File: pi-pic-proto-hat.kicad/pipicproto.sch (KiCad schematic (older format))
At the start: 34 parts, among them J1 RUN/~PGM~, J10 Conn_01x13_Male, J11 Conn_5P_2, J12 Conn_01x01_Male, J2 Conn_SW1, J22 Conn_01x13_Male, J3 Conn_5P, J4 Conn_3V3P, J5 Conn_3V3P_2, J6 Barrel_Jack_Switch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

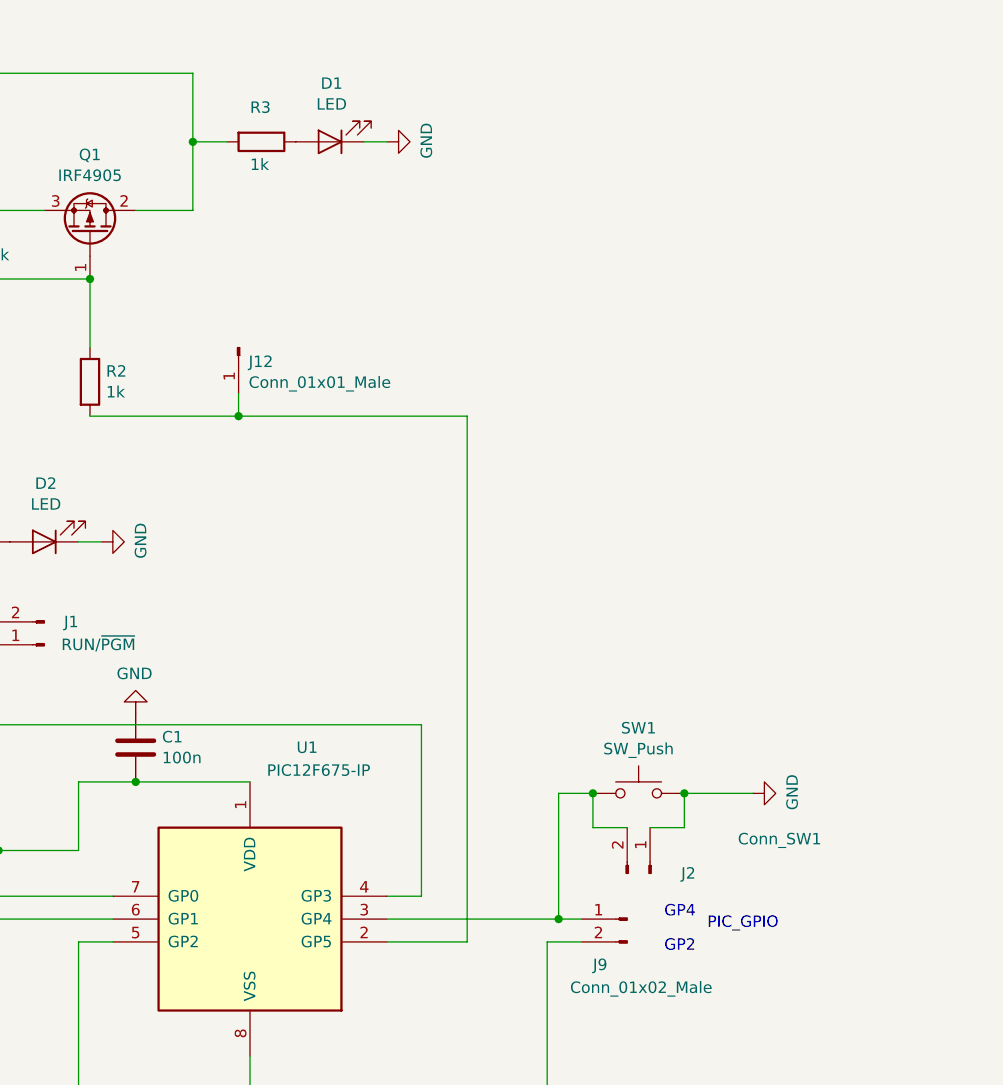
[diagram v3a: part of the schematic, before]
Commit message: V2.20: added DS3231
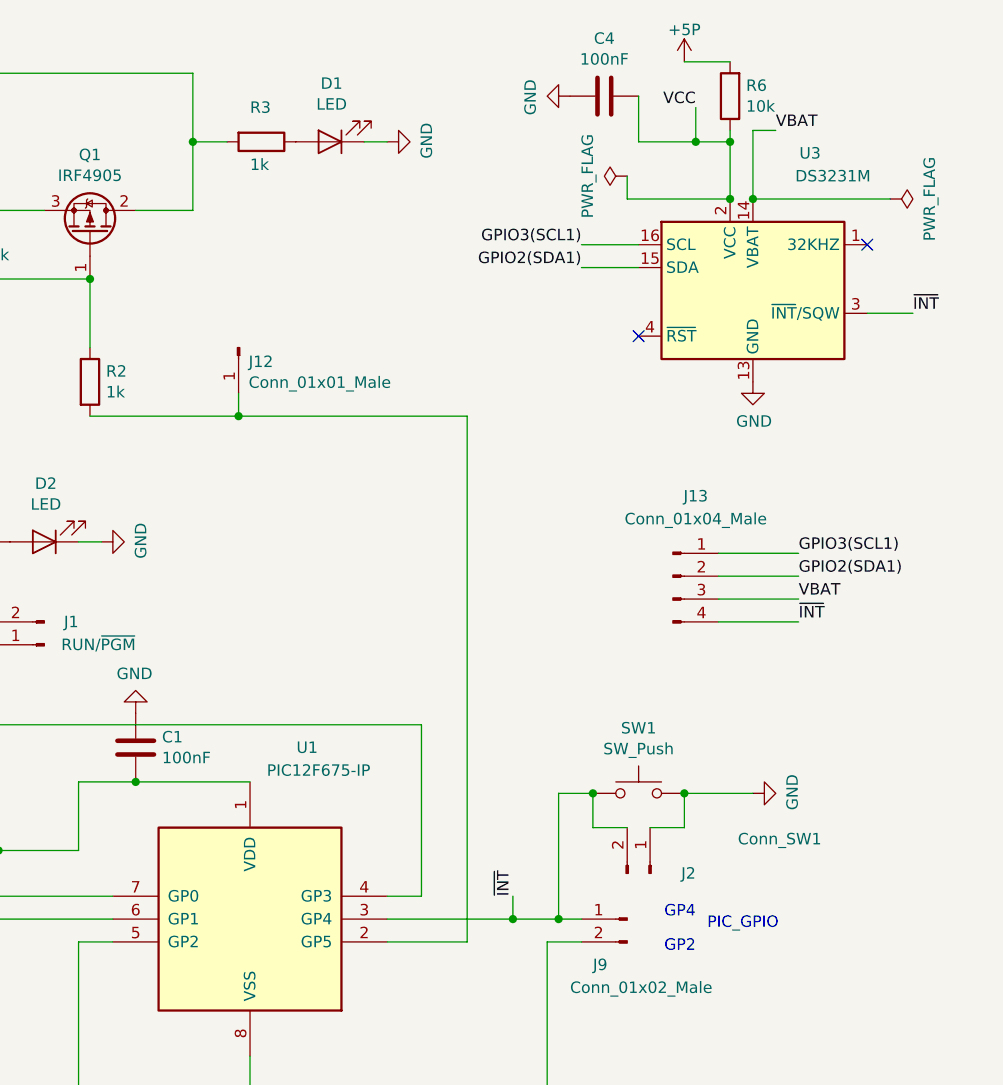
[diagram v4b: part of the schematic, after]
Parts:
- added C4: 100nF, Capacitor_SMD:C_1206_3216Metric_Pad1.42x1.75mm_HandSolder, symbol Device:C
- added J13: Conn_01x04_Male, Connector_PinHeader_2.54mm:PinHeader_1x04_P2.54mm_Vertical, symbol Connector:Conn_01x04_Male
- added R6: 10k, Resistor_SMD:R_1206_3216Metric_Pad1.42x1.75mm_HandSolder, symbol Device:R
- added U3: DS3231M, Package_SO:SOIC-16W_7.5x10.3mm_P1.27mm, symbol Timer_RTC:DS3231M
- C1: value 100n -> 100nF
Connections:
- net +5P: now also R6.2
- net GND: now also C4.2, U3.10 (GND), U3.11 (GND), U3.12 (GND), U3.13 (GND), U3.5 (GND), U3.6 (GND), U3.7 (GND), U3.8 (GND), U3.9 (GND)
- net GPIO2(SDA1): now also J13.2 (Pin_2), U3.15 (SDA)
- net GPIO3(SCL1): now also J13.1 (Pin_1), U3.16 (SCL)
- net ~INT: now reaches J2.2 (Pin_2), J9.1 (Pin_1), SW1.1, U1.3 (GP4)
- net ~INT: now also J13.4 (Pin_4), U3.3 (~INT~/SQW)
- new net VBAT: J13.3 (Pin_3), U3.14 (VBAT)
- new net VCC: C4.1, R6.1, U3.2 (VCC)
- no-connect marks 4 -> 6
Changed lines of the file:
@@
 Sheet 1 1
 Title "PI PIC Prototyping Area"
-Date "2020-07-25"
-Rev "2.19"
+Date "2020-07-30"
+Rev "2.20"
 Comp "Bernhard Bablok, Lothar Hiller"
 Comment1 "https://github.com/bablokb/pi-pic-proto-hat"
@@
 P 7500 3850
 F 0 "C1" H 7615 3896 50  0000 L CNN
-F 1 "100n" H 7615 3805 50  0000 L CNN
+F 1 "100nF" H 7615 3805 50  0000 L CNN
 F 2 "Capacitor_SMD:C_1206_3216Metric_Pad1.42x1.75mm_HandSolder" H 7538 3700 50  0001 C CNN
 F 3 "~" H 7500 3850 50  0001 C CNN
@@
 $EndComp
 Wire Wire Line
-	8600 4600 9350 4600
+	8600 4600 9150 4600
 Wire Wire Line
 	9300 5750 9300 4700
@@
 Wire Wire Line
 	7950 2400 7300 2400
+$Comp
+L Timer_RTC:DS3231M U3
+U 1 1 5F238501
+P 10200 1850
+F 0 "U3" H 10450 2450 50  0000 C CNN
+F 1 "DS3231M" H 10550 2350 50  0000 C CNN
+F 2 "Package_SO:SOIC-16W_7.5x10.3mm_P1.27mm" H 10200 1250 50  0001 C CNN
+F 3 "http://datasheets.maximintegrated.com/en/ds/DS3231.pdf" H 10470 1900 50  0001 C CNN
+	1    10200 1850
+	1    0    0    -1
+$EndComp
+$Comp
+L Connector:Conn_01x04_Male J13
+U 1 1 5F2395D8
+P 9850 3100
+F 0 "J13" H 9950 3450 50  0000 C CNN
+F 1 "Conn_01x04_Male" H 9950 3350 50  0000 C CNN
+F 2 "Connector_PinHeader_2.54mm:PinHeader_1x04_P2.54mm_Vertical" H 9850 3100 50  0001 C CNN
+F 3 "~" H 9850 3100 50  0001 C CNN
+	1    9850 3100
+	1    0    0    -1
+$EndComp
+Text Label 10400 3100 0    50   ~ 0
+GPIO2(SDA1)
+Text Label 10400 3000 0    50   ~ 0
+GPIO3(SCL1)
+Text Label 9450 1750 2    50   ~ 0
+GPIO2(SDA1)
+Text Label 9450 1650 2    50   ~ 0
+GPIO3(SCL1)
+Text Label 10400 3300 0    50   ~ 0
+~INT
+Text Label 10900 1950 0    50   ~ 0
+~INT
+NoConn ~ 10700 1650
+$Comp
+L power:GND #PWR013
+U 1 1 5F24DB44
+P 10200 2250
+F 0 "#PWR013" H 10200 2000 50  0001 C CNN
+F 1 "GND" H 10205 2077 50  0000 C CNN
+F 2 "" H 10200 2250 50  0001 C CNN
+F 3 "" H 10200 2250 50  0001 C CNN
+	1    10200 2250
+	1    0    0    -1
+$EndComp
+NoConn ~ 9700 2050
+$Comp
+L Device:R R6
+U 1 1 5F25761B
+P 10100 1000
+F 0 "R6" H 10030 954 50  0000 R CNN
+F 1 "10k" H 10030 1045 50  0000 R CNN
+F 2 "Resistor_SMD:R_1206_3216Metric_Pad1.42x1.75mm_HandSolder" V 10030 1000 50  0001 C CNN
+F 3 "~" H 10100 1000 50  0001 C CNN
+	1    10100 1000
+	-1   0    0    1
+$EndComp
+$Comp
+L power:+5P #PWR012
+U 1 1 5F26109E
+P 9900 850
+F 0 "#PWR012" H 9900 700 50  0001 C CNN
+F 1 "+5P" H 9900 990 50  0000 C CNN
+F 2 "" H 9900 850 50  0000 C CNN
+F 3 "" H 9900 850 50  0000 C CNN
+	1    9900 850
+	1    0    0    -1
+$EndComp
+Wire Wire Line
+	9900 850  10100 850
+Wire Wire Line
+	10700 1950 10900 1950
+Wire Wire Line
+	10050 3100 10400 3100
+Wire Wire Line
+	10050 3000 10400 3000
+Wire Wire Line
+	9700 1650 9450 1650
+Wire Wire Line
+	9700 1750 9450 1750
+Text Label 10400 3200 0    50   ~ 0
+VBAT
+Text Label 10300 1150 0    50   ~ 0
+VBAT
+Wire Wire Line
+	10200 1450 10200 1150
+Wire Wire Line
+	10200 1150 10300 1150
+Wire Wire Line
+	10400 3200 10050 3200
+Text Label 9950 1050 2    50   ~ 0
+VCC
+Wire Wire Line
+	10050 3300 10400 3300
+$Comp
+L power:PWR_FLAG #FLG0103
+U 1 1 5F2E32E1
+P 9650 1350
+F 0 "#FLG0103" H 9650 1425 50  0001 C CNN
+F 1 "PWR_FLAG" H 9650 1523 50  0000 C CNN
+F 2 "" H 9650 1350 50  0001 C CNN
+F 3 "~" H 9650 1350 50  0001 C CNN
+	1    9650 1350
+	0    -1   -1   0
+$EndComp
+Wire Wire Line
+	9650 1350 9650 1450
+Wire Wire Line
+	9650 1450 10100 1450
+Connection ~ 10100 1450
+$Comp
+L power:PWR_FLAG #FLG0104
+U 1 1 5F2EE834
+P 10800 1450
+F 0 "#FLG0104" H 10800 1525 50  0001 C CNN
+F 1 "PWR_FLAG" H 10800 1623 50  0000 C CNN
+F 2 "" H 10800 1450 50  0001 C CNN
+F 3 "~" H 10800 1450 50  0001 C CNN
+	1    10800 1450
+	0    1    1    0
+$EndComp
+Wire Wire Line
+	10800 1450 10200 1450
+Connection ~ 10200 1450
+$Comp
+L Device:C C4
+U 1 1 5F313C7C
+P 9550 1000
+F 0 "C4" V 9298 1000 50  0000 C CNN
+F 1 "100nF" V 9389 1000 50  0000 C CNN
+F 2 "Capacitor_SMD:C_1206_3216Metric_Pad1.42x1.75mm_HandSolder" H 9588 850 50  0001 C CNN
+F 3 "~" H 9550 1000 50  0001 C CNN
+	1    9550 1000
+	0    1    1    0
+$EndComp
+Wire Wire Line
+	10100 1150 10100 1200
+Wire Wire Line
+	9950 1050 9950 1200
+Wire Wire Line
+	9950 1200 10100 1200
+Connection ~ 10100 1200
+Wire Wire Line
+	10100 1200 10100 1450
+Wire Wire Line
+	9700 1000 9700 1200
+Wire Wire Line
+	9700 1200 9950 1200
+Connection ~ 9950 1200
+$Comp
+L power:GND #PWR023
+U 1 1 5F34D64A
+P 9400 1000
+F 0 "#PWR023" H 9400 750 50  0001 C CNN
+F 1 "GND" H 9405 827 50  0000 C CNN
+F 2 "" H 9400 1000 50  0001 C CNN
+F 3 "" H 9400 1000 50  0001 C CNN
+	1    9400 1000
+	0    1    1    0
+$EndComp
+Text Label 9150 4500 1    50   ~ 0
+~INT
+Wire Wire Line
+	9150 4500 9150 4600
+Connection ~ 9150 4600
+Wire Wire Line
+	9150 4600 9350 4600
 $EndSCHEMATC

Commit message: V2.21: added 32KHZ-pin of RTC to connector
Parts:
- J13: value Conn_01x04_Male -> Conn_01x05_Male; footprint Connector_PinHeader_2.54mm:PinHeader_1x04_P2.54mm_Vertical -> Connector_PinHeader_2.54mm:PinHeader_1x05_P2.54mm_Vertical; symbol Connector:Conn_01x04_Male -> Connector:Conn_01x05_Male
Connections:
- net 32KHZ: now reaches U3.1 (32KHZ)
- net 32KHZ: now also J13.5 (Pin_5)
- no-connect marks 6 -> 5
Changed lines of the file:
@@
 Sheet 1 1
 Title "PI PIC Prototyping Area"
-Date "2020-07-30"
-Rev "2.20"
+Date "2020-08-01"
+Rev "2.21"
 Comp "Bernhard Bablok, Lothar Hiller"
 Comment1 "https://github.com/bablokb/pi-pic-proto-hat"
@@
 U 1 1 5F238501
 P 10200 1850
-F 0 "U3" H 10450 2450 50  0000 C CNN
-F 1 "DS3231M" H 10550 2350 50  0000 C CNN
+F 0 "U3" H 10350 2300 50  0000 C CNN
+F 1 "DS3231M" H 10450 2200 50  0000 C CNN
 F 2 "Package_SO:SOIC-16W_7.5x10.3mm_P1.27mm" H 10200 1250 50  0001 C CNN
 F 3 "http://datasheets.maximintegrated.com/en/ds/DS3231.pdf" H 10470 1900 50  0001 C CNN
@@
 $EndComp
 $Comp
-L Connector:Conn_01x04_Male J13
+L Connector:Conn_01x05_Male J13
 U 1 1 5F2395D8
-P 9850 3100
-F 0 "J13" H 9950 3450 50  0000 C CNN
-F 1 "Conn_01x04_Male" H 9950 3350 50  0000 C CNN
-F 2 "Connector_PinHeader_2.54mm:PinHeader_1x04_P2.54mm_Vertical" H 9850 3100 50  0001 C CNN
-F 3 "~" H 9850 3100 50  0001 C CNN
-	1    9850 3100
+P 9850 3200
+F 0 "J13" H 9950 3600 50  0000 C CNN
+F 1 "Conn_01x05_Male" H 9950 3500 50  0000 C CNN
+F 2 "Connector_PinHeader_2.54mm:PinHeader_1x05_P2.54mm_Vertical" H 9850 3200 50  0001 C CNN
+F 3 "~" H 9850 3200 50  0001 C CNN
+	1    9850 3200
 	1    0    0    -1
 $EndComp
@@
 Text Label 10900 1950 0    50   ~ 0
 ~INT
-NoConn ~ 10700 1650
 $Comp
 L power:GND #PWR013
@@
 P 10800 1450
 F 0 "#FLG0104" H 10800 1525 50  0001 C CNN
-F 1 "PWR_FLAG" H 10800 1623 50  0000 C CNN
+F 1 "PWR_FLAG" V 10700 1600 50  0000 C CNN
 F 2 "" H 10800 1450 50  0001 C CNN
 F 3 "~" H 10800 1450 50  0001 C CNN
@@
 Wire Wire Line
 	9150 4600 9350 4600
+Text Label 10400 3400 0    50   ~ 0
+32KHZ
+Wire Wire Line
+	10050 3400 10400 3400
+Text Label 10900 1650 0    50   ~ 0
+32KHZ
+Wire Wire Line
+	10700 1650 10900 1650
 $EndSCHEMATC

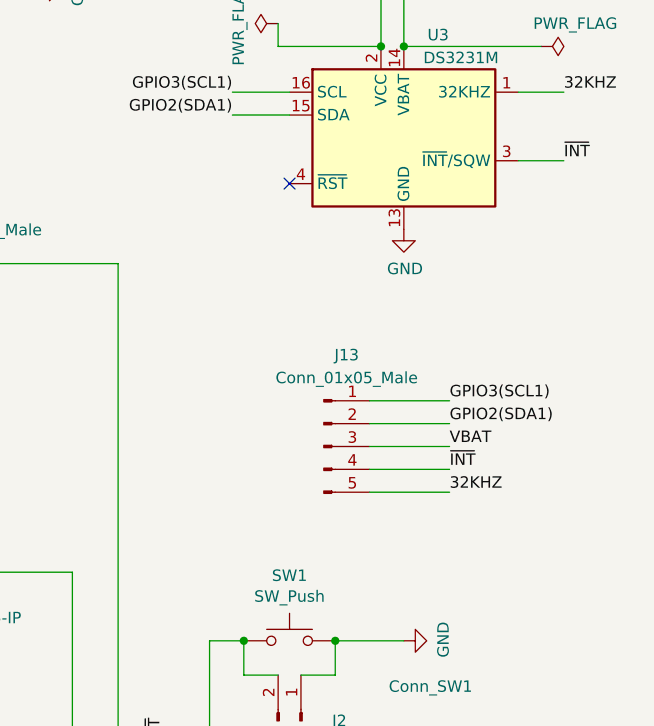
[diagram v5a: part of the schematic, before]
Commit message: V2.22: added RST/GND connector for RTC
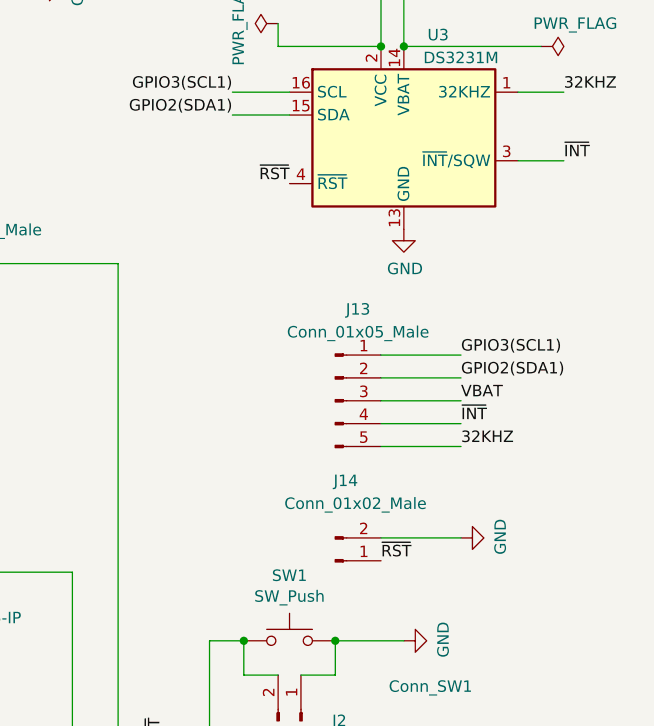
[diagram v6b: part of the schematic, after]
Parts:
- added J14: Conn_01x02_Male, Connector_PinHeader_2.54mm:PinHeader_1x02_P2.54mm_Vertical, symbol Connector:Conn_01x02_Male
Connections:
- net GND: now also J14.2 (Pin_2)
- net ~RST: now reaches U3.4 (~RST)
- net ~RST: now also J14.1 (Pin_1)
- no-connect marks 5 -> 4
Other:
- moved on the sheet: J13
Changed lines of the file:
@@
 Title "PI PIC Prototyping Area"
 Date "2020-08-01"
-Rev "2.21"
+Rev "2.22"
 Comp "Bernhard Bablok, Lothar Hiller"
 Comment1 "https://github.com/bablokb/pi-pic-proto-hat"
@@
 L Connector:Conn_01x05_Male J13
 U 1 1 5F2395D8
-P 9850 3200
-F 0 "J13" H 9950 3600 50  0000 C CNN
-F 1 "Conn_01x05_Male" H 9950 3500 50  0000 C CNN
-F 2 "Connector_PinHeader_2.54mm:PinHeader_1x05_P2.54mm_Vertical" H 9850 3200 50  0001 C CNN
-F 3 "~" H 9850 3200 50  0001 C CNN
-	1    9850 3200
-	1    0    0    -1
-$EndComp
-Text Label 10400 3100 0    50   ~ 0
+P 9900 3000
+F 0 "J13" H 10000 3400 50  0000 C CNN
+F 1 "Conn_01x05_Male" H 10000 3300 50  0000 C CNN
+F 2 "Connector_PinHeader_2.54mm:PinHeader_1x05_P2.54mm_Vertical" H 9900 3000 50  0001 C CNN
+F 3 "~" H 9900 3000 50  0001 C CNN
+	1    9900 3000
+	1    0    0    -1
+$EndComp
+Text Label 10450 2900 0    50   ~ 0
 GPIO2(SDA1)
-Text Label 10400 3000 0    50   ~ 0
+Text Label 10450 2800 0    50   ~ 0
 GPIO3(SCL1)
 Text Label 9450 1750 2    50   ~ 0
@@
 Text Label 9450 1650 2    50   ~ 0
 GPIO3(SCL1)
-Text Label 10400 3300 0    50   ~ 0
+Text Label 10450 3100 0    50   ~ 0
 ~INT
 Text Label 10900 1950 0    50   ~ 0
@@
 	1    0    0    -1
 $EndComp
-NoConn ~ 9700 2050
 $Comp
 L Device:R R6
@@
 	10700 1950 10900 1950
 Wire Wire Line
-	10050 3100 10400 3100
-Wire Wire Line
-	10050 3000 10400 3000
+	10100 2900 10450 2900
+Wire Wire Line
+	10100 2800 10450 2800
 Wire Wire Line
 	9700 1650 9450 1650
 Wire Wire Line
 	9700 1750 9450 1750
-Text Label 10400 3200 0    50   ~ 0
+Text Label 10450 3000 0    50   ~ 0
 VBAT
 Text Label 10300 1150 0    50   ~ 0
@@
 	10200 1150 10300 1150
 Wire Wire Line
-	10400 3200 10050 3200
+	10450 3000 10100 3000
 Text Label 9950 1050 2    50   ~ 0
 VCC
 Wire Wire Line
-	10050 3300 10400 3300
+	10100 3100 10450 3100
 $Comp
 L power:PWR_FLAG #FLG0103
@@
 Wire Wire Line
 	9150 4600 9350 4600
-Text Label 10400 3400 0    50   ~ 0
+Text Label 10450 3200 0    50   ~ 0
 32KHZ
 Wire Wire Line
-	10050 3400 10400 3400
+	10100 3200 10450 3200
 Text Label 10900 1650 0    50   ~ 0
 32KHZ
 Wire Wire Line
 	10700 1650 10900 1650
+$Comp
+L Connector:Conn_01x02_Male J14
+U 1 1 5F2F400C
+P 9900 3700
+F 0 "J14" H 10000 3350 50  0000 R CNN
+F 1 "Conn_01x02_Male" H 10300 3450 50  0000 R CNN
+F 2 "Connector_PinHeader_2.54mm:PinHeader_1x02_P2.54mm_Vertical" H 9900 3700 50  0001 C CNN
+F 3 "~" H 9900 3700 50  0001 C CNN
+	1    9900 3700
+	1    0    0    1
+$EndComp
+Text Label 10100 3700 0    50   ~ 0
+~RST
+$Comp
+L power:GND #PWR022
+U 1 1 5F3365CF
+P 10450 3600
+F 0 "#PWR022" H 10450 3350 50  0001 C CNN
+F 1 "GND" H 10455 3427 50  0000 C CNN
+F 2 "" H 10450 3600 50  0001 C CNN
+F 3 "" H 10450 3600 50  0001 C CNN
+	1    10450 3600
+	0    -1   -1   0
+$EndComp
+Wire Wire Line
+	10100 3600 10450 3600
+Text Label 9700 2050 2    50   ~ 0
+~RST
 $EndSCHEMATC
